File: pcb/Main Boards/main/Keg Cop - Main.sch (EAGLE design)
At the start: 6 parts, among them X2 RJ45-8X

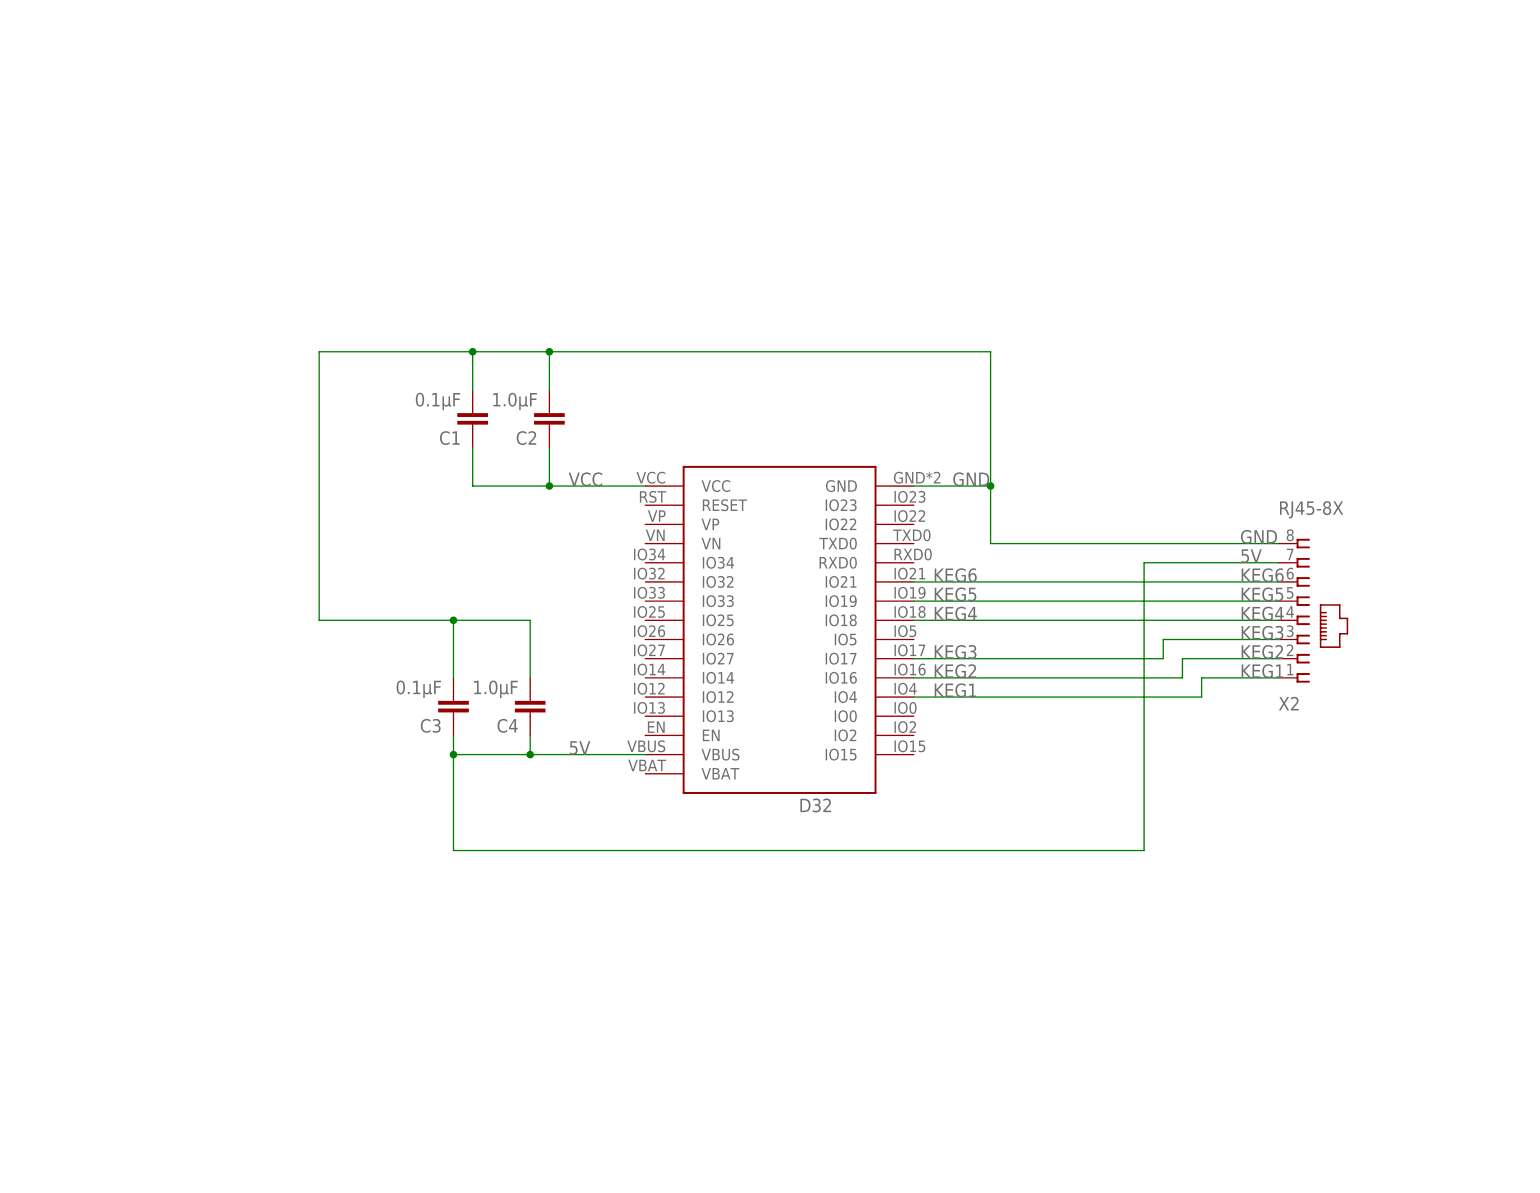
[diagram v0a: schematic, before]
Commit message: Rewire, move to 9 meters
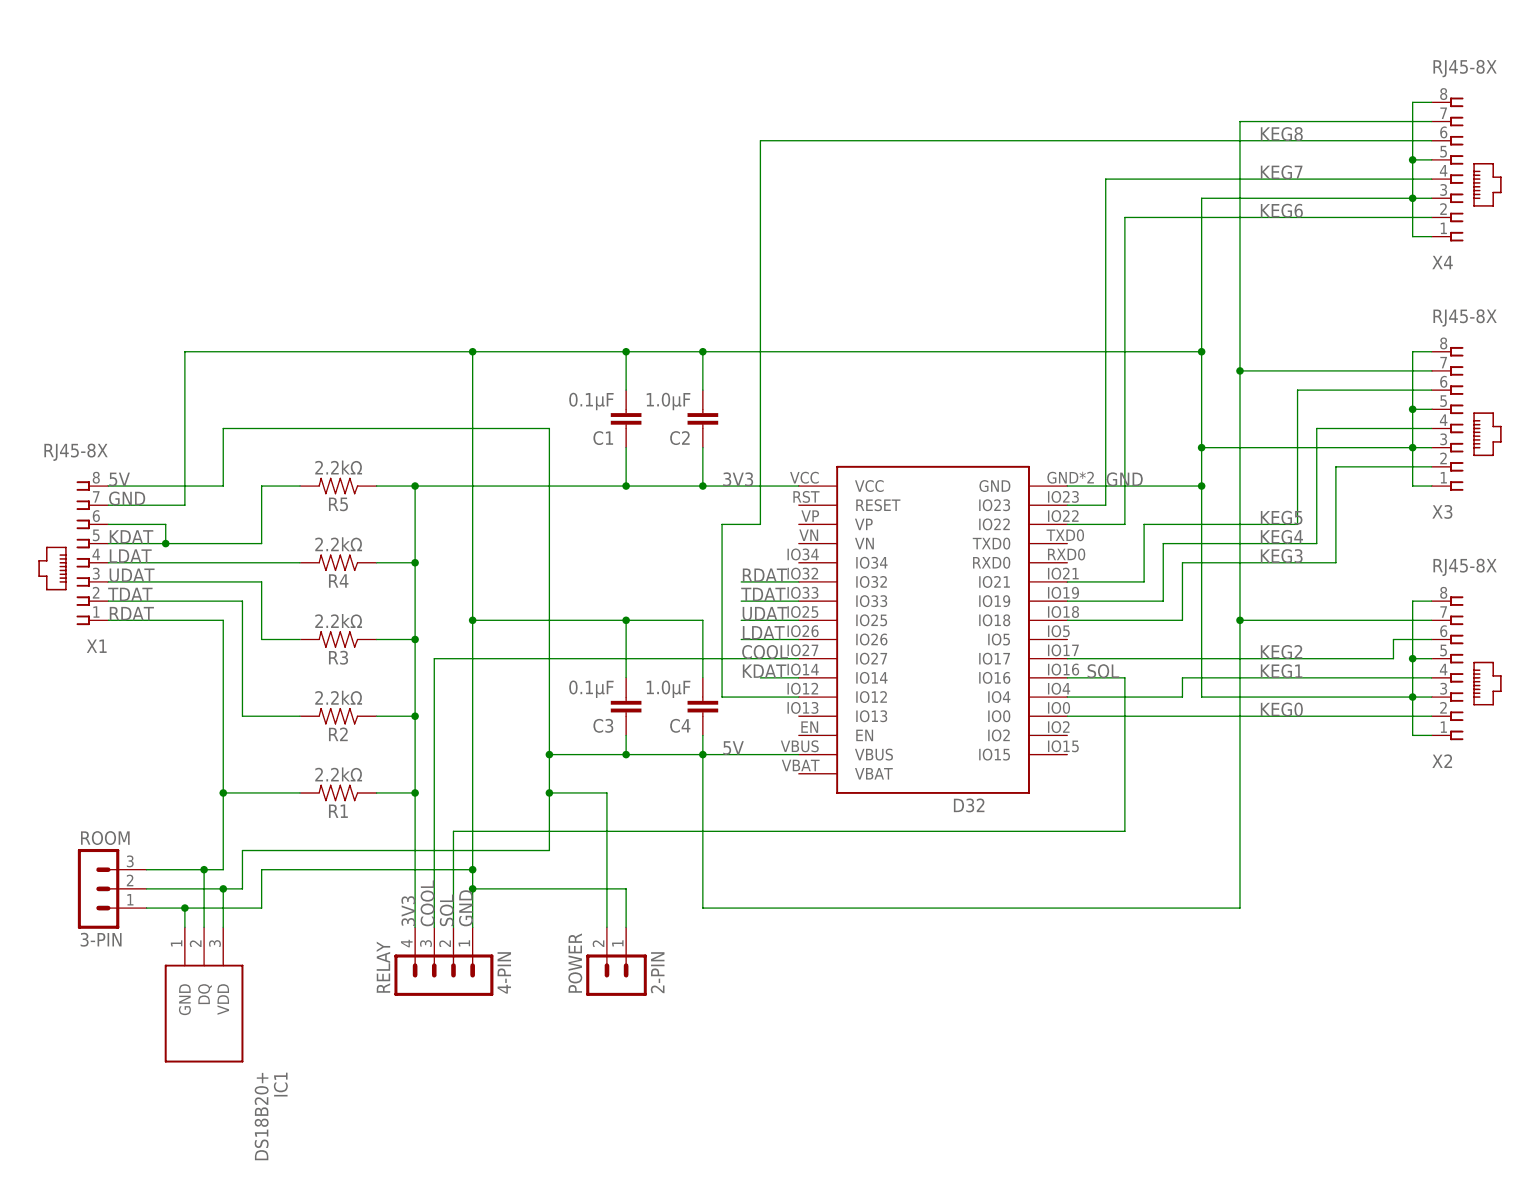
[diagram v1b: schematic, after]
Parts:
- added IC1: DS18B20+, SamacSys_Parts:DS18B20+
- added POWER: 2-PIN, Donnie:HDR-2
- added R1, R2, R3, R4, R5: 2.2kΩ, SparkFun-Resistors:RESISTORAXIAL-0.3
- added RELAY: 4-PIN, Donnie:MA04-1
- added ROOM: 3-PIN, Donnie:HDR-3
- added X1, X3, X4: RJ45-8X, con-tycoelectronics:RJ45-8X
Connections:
- removed net VCC: C1.1, C2.1, D32.VCC
- new net 3V3: C1.1, C2.1, D32.VCC, R1.1, R2.1, R3.1, R4.1, R5.1, RELAY.4
- new net COOL: D32.IO27, RELAY.3
- new net KDAT: D32.IO14, R5.2, X1.5, X1.6
- new net KEG0: D32.IO0, X2.2
- new net KEG7: D32.IO23, X4.4
- new net KEG8: D32.IO12, X4.6
- new net LDAT: D32.IO26, R4.2, X1.4
- new net RDAT: D32.IO32, IC1.DQ, R1.2, ROOM.3, X1.1
- new net SOL: D32.IO16, RELAY.2
- new net TDAT: D32.IO33, R2.2, X1.2
- new net UDAT: D32.IO25, R3.2, X1.3
- net 5V: now also IC1.VDD, POWER.2, ROOM.2, X1.8, X3.7, X4.7
- net GND: now also IC1.GND, POWER.1, RELAY.1, ROOM.1, X1.7, X2.1, X2.3, X2.5, X3.1, X3.3, X3.5, X3.8, X4.1, X4.3, X4.5, X4.8
- net KEG1: now also X2.4; no longer X2.1
- net KEG2: now also D32.IO17, X2.6; no longer D32.IO16, X2.2
- net KEG3: now also D32.IO18, X3.2; no longer D32.IO17, X2.3
- net KEG4: now also D32.IO19, X3.4; no longer D32.IO18, X2.4
- net KEG5: now also D32.IO21, X3.6; no longer D32.IO19, X2.5
- net KEG6: now also D32.IO22, X4.2; no longer D32.IO21, X2.6
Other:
- moved on the sheet: C1, C2, C3, C4, D32, X2

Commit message: Add pullups, move KEG0 to GPIO13
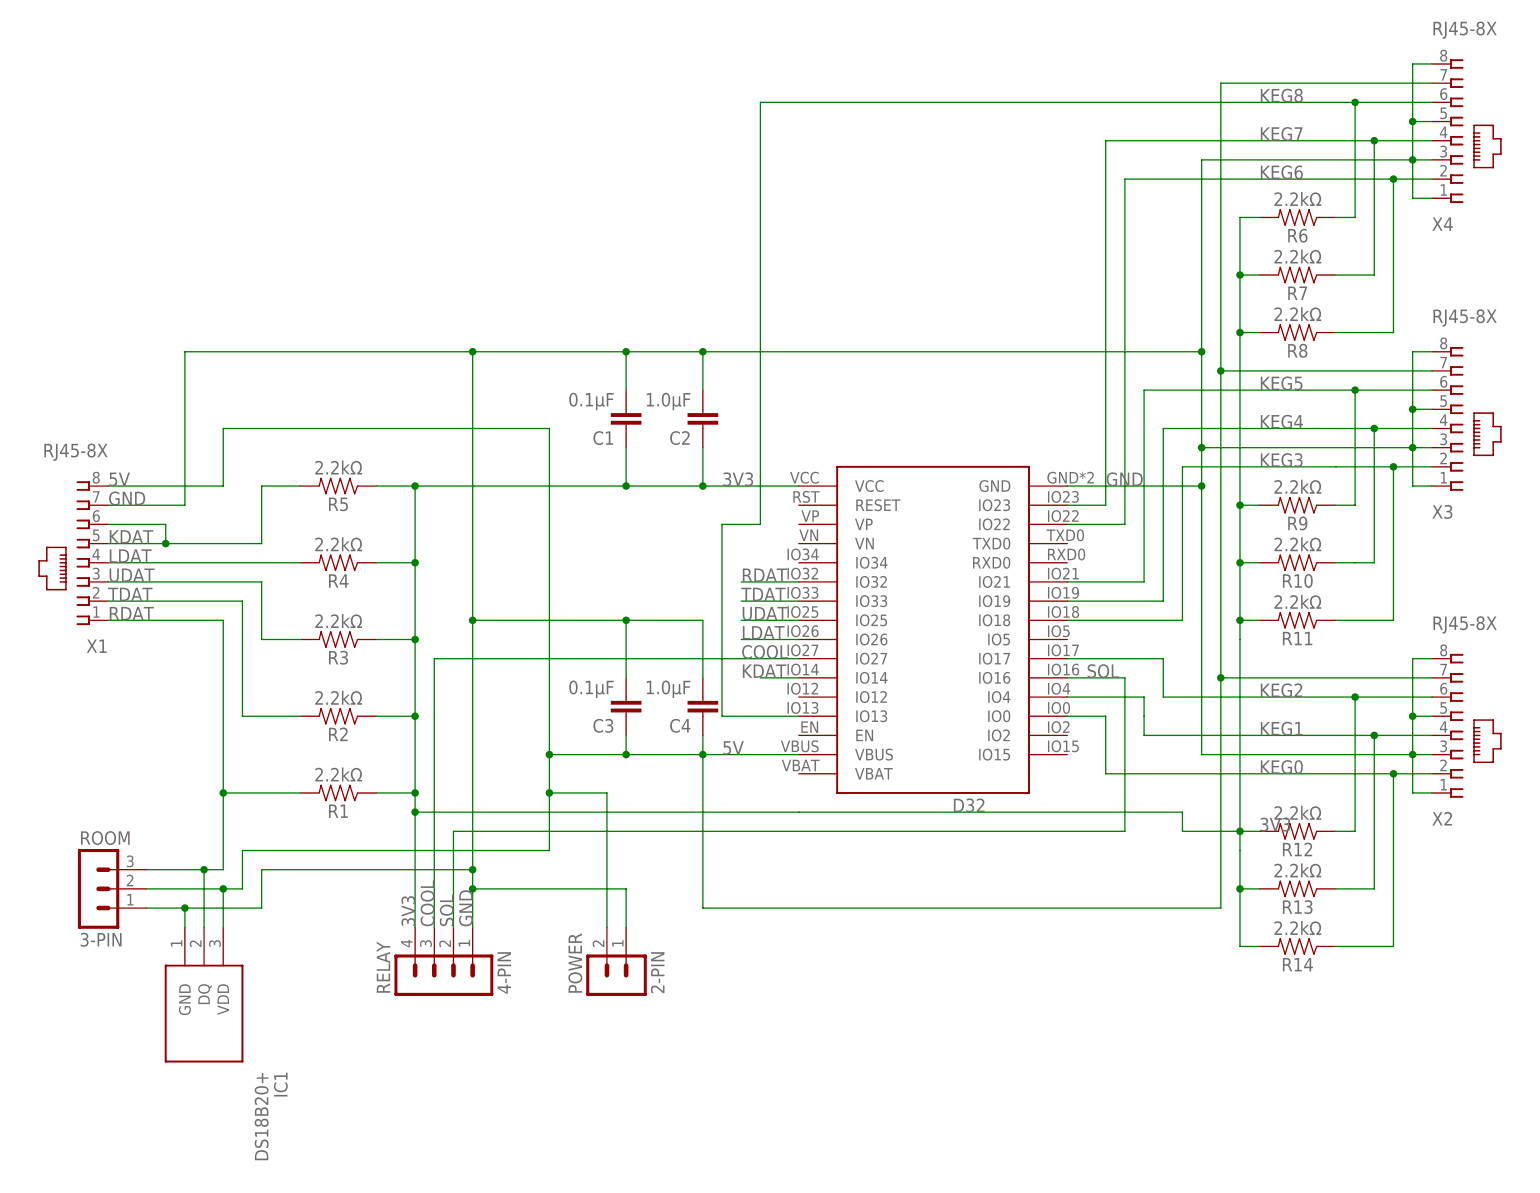
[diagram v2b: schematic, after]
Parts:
- added R10, R11, R12, R13, R14, R6, R7, R8, R9: 2.2kΩ, SparkFun-Resistors:RESISTORAXIAL-0.3
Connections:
- net 3V3: now also R10.2, R11.2, R12.2, R13.2, R14.2, R6.2, R7.2, R8.2, R9.2
- net KEG0: now also R14.1
- net KEG1: now also R13.1
- net KEG2: now also R12.1
- net KEG3: now also R11.1
- net KEG4: now also R10.1
- net KEG5: now also R9.1
- net KEG6: now also R8.1
- net KEG7: now also R7.1
- net KEG8: now also D32.IO13, R6.1; no longer D32.IO12
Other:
- moved on the sheet: X2, X4

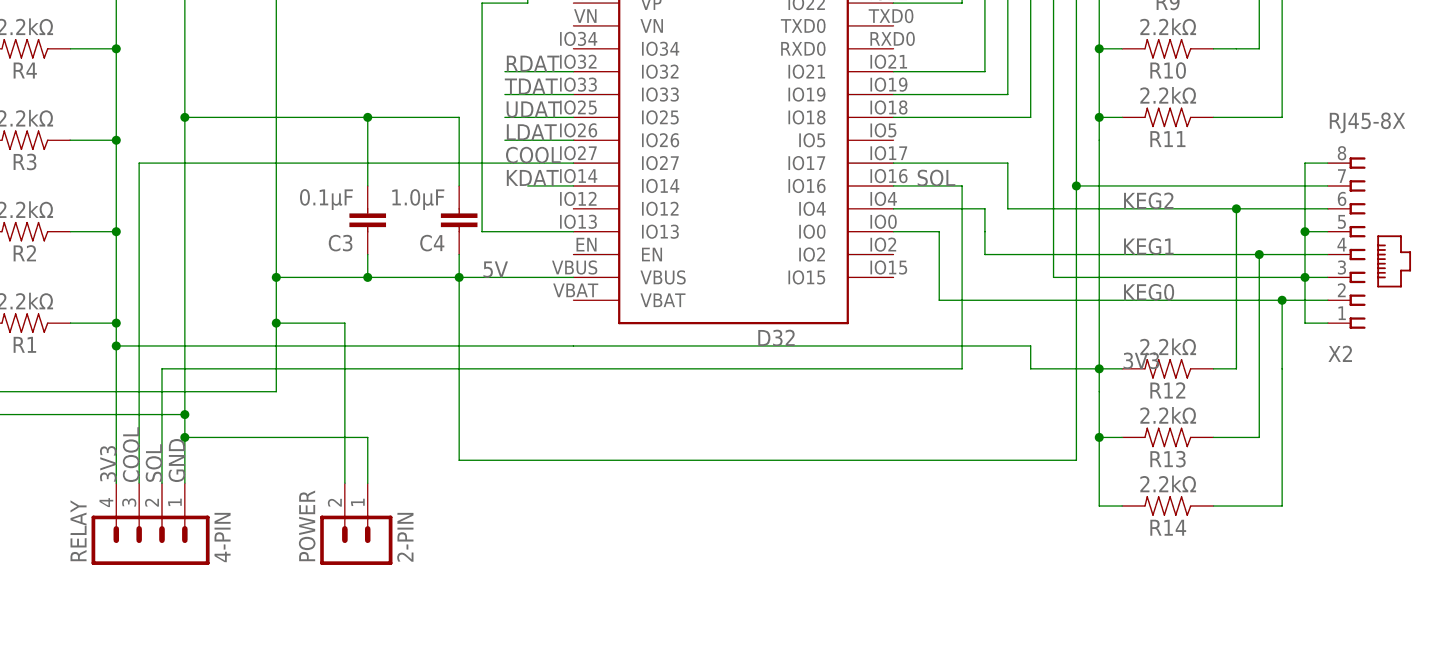
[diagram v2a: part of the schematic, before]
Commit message: K0 to 4 K1 to 16 SOL to 2
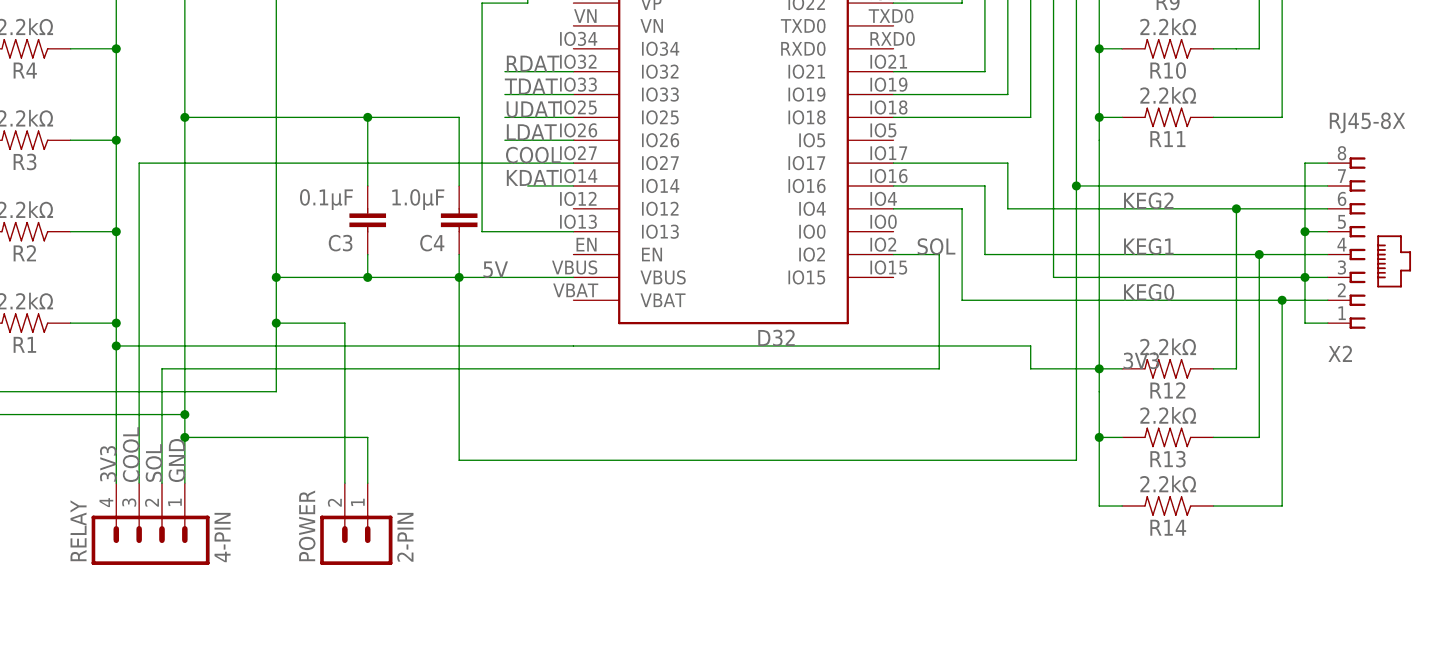
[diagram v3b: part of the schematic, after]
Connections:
- net KEG0: now also D32.IO4; no longer D32.IO0
- net KEG1: now also D32.IO16; no longer D32.IO4
- net SOL: now also D32.IO2; no longer D32.IO16
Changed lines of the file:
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@@
 <pinref part="RELAY" gate="1" pin="2"/>
 <wire x1="-27.94" y1="10.16" x2="-27.94" y2="22.86" width="0.1524" layer="91"/>
-<wire x1="-27.94" y1="22.86" x2="60.96" y2="22.86" width="0.1524" layer="91"/>
-<wire x1="60.96" y1="22.86" x2="60.96" y2="43.18" width="0.1524" layer="91"/>
-<pinref part="D32" gate="G$1" pin="IO16"/>
-<wire x1="60.96" y1="43.18" x2="53.34" y2="43.18" width="0.1524" layer="91"/>
+<wire x1="-27.94" y1="22.86" x2="58.42" y2="22.86" width="0.1524" layer="91"/>
 <label x="-27.94" y="10.16" size="1.778" layer="95" rot="R90"/>
-<label x="55.88" y="43.18" size="1.778" layer="95"/>
+<label x="55.88" y="35.56" size="1.778" layer="95"/>
+<wire x1="58.42" y1="22.86" x2="58.42" y2="35.56" width="0.1524" layer="91"/>
+<pinref part="D32" gate="G$1" pin="IO2"/>
+<wire x1="58.42" y1="35.56" x2="53.34" y2="35.56" width="0.1524" layer="91"/>
 </segment>
 </net>
@@
 <net name="KEG0" class="0">
 <segment>
-<pinref part="D32" gate="G$1" pin="IO0"/>
 <pinref part="X2" gate="G$1" pin="2"/>
-<wire x1="53.34" y1="38.1" x2="58.42" y2="38.1" width="0.1524" layer="91"/>
-<wire x1="58.42" y1="38.1" x2="58.42" y2="30.48" width="0.1524" layer="91"/>
-<wire x1="58.42" y1="30.48" x2="96.52" y2="30.48" width="0.1524" layer="91"/>
+<wire x1="60.96" y1="40.64" x2="60.96" y2="30.48" width="0.1524" layer="91"/>
+<wire x1="60.96" y1="30.48" x2="96.52" y2="30.48" width="0.1524" layer="91"/>
 <label x="78.74" y="30.48" size="1.778" layer="95"/>
 <pinref part="R14" gate="G$1" pin="1"/>
 <wire x1="96.52" y1="30.48" x2="101.6" y2="30.48" width="0.1524" layer="91"/>
-<wire x1="96.52" y1="22.86" x2="96.52" y2="30.48" width="0.1524" layer="91"/>
 <junction x="96.52" y="30.48"/>
-<wire x1="96.52" y1="22.86" x2="96.52" y2="7.62" width="0.1524" layer="91"/>
+<wire x1="96.52" y1="30.48" x2="96.52" y2="7.62" width="0.1524" layer="91"/>
 <wire x1="96.52" y1="7.62" x2="88.9" y2="7.62" width="0.1524" layer="91"/>
+<pinref part="D32" gate="G$1" pin="IO4"/>
+<wire x1="53.34" y1="40.64" x2="60.96" y2="40.64" width="0.1524" layer="91"/>
 </segment>
 </net>
@@
 <pinref part="X2" gate="G$1" pin="4"/>
 <wire x1="101.6" y1="35.56" x2="93.98" y2="35.56" width="0.1524" layer="91"/>
-<pinref part="D32" gate="G$1" pin="IO4"/>
 <label x="78.74" y="35.56" size="1.778" layer="95"/>
 <pinref part="R13" gate="G$1" pin="1"/>
@@
 <wire x1="93.98" y1="15.24" x2="93.98" y2="35.56" width="0.1524" layer="91"/>
 <junction x="93.98" y="35.56"/>
-<wire x1="53.34" y1="40.64" x2="63.5" y2="40.64" width="0.1524" layer="91"/>
-<wire x1="63.5" y1="40.64" x2="63.5" y2="38.1" width="0.1524" layer="91"/>
-<wire x1="63.5" y1="38.1" x2="63.5" y2="35.56" width="0.1524" layer="91"/>
+<wire x1="63.5" y1="43.18" x2="63.5" y2="35.56" width="0.1524" layer="91"/>
 <wire x1="63.5" y1="35.56" x2="93.98" y2="35.56" width="0.1524" layer="91"/>
+<pinref part="D32" gate="G$1" pin="IO16"/>
+<wire x1="53.34" y1="43.18" x2="63.5" y2="43.18" width="0.1524" layer="91"/>
 </segment>
 </net>
